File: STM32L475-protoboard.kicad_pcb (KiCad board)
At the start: 4 copper layers, 73.6 x 52.9 mm, 67 parts, among them J1 USB_HEADER, J10 Conn_01x02_Male, J11 SD_Card, J2 USB_B_Micro, J3 DCin, J5 W5500_ETHERNET, J6 STLINK2, J7 BOOT_MODE, J8 Conn_02x20_Odd_Even, J9 Conn_01x02_Male, SW1 RESET, U1 SRV05-4, U2 AMS1117-3.3, U3 STM32L475RCTx, Y1 Crystal_GND24, Y2 32.768k

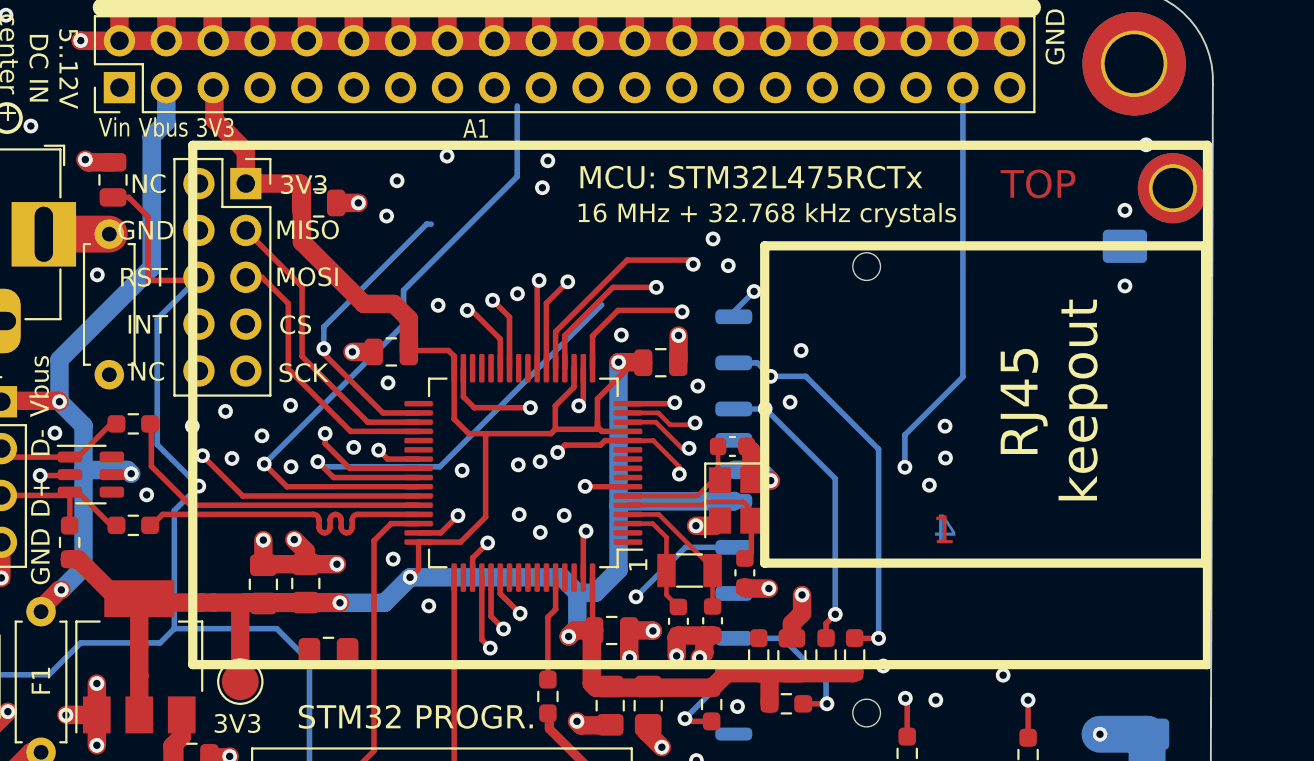
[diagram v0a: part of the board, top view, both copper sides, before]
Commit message: STM32L475 should have internal pullup for USB line, but need to be checked (now DNP resistor)
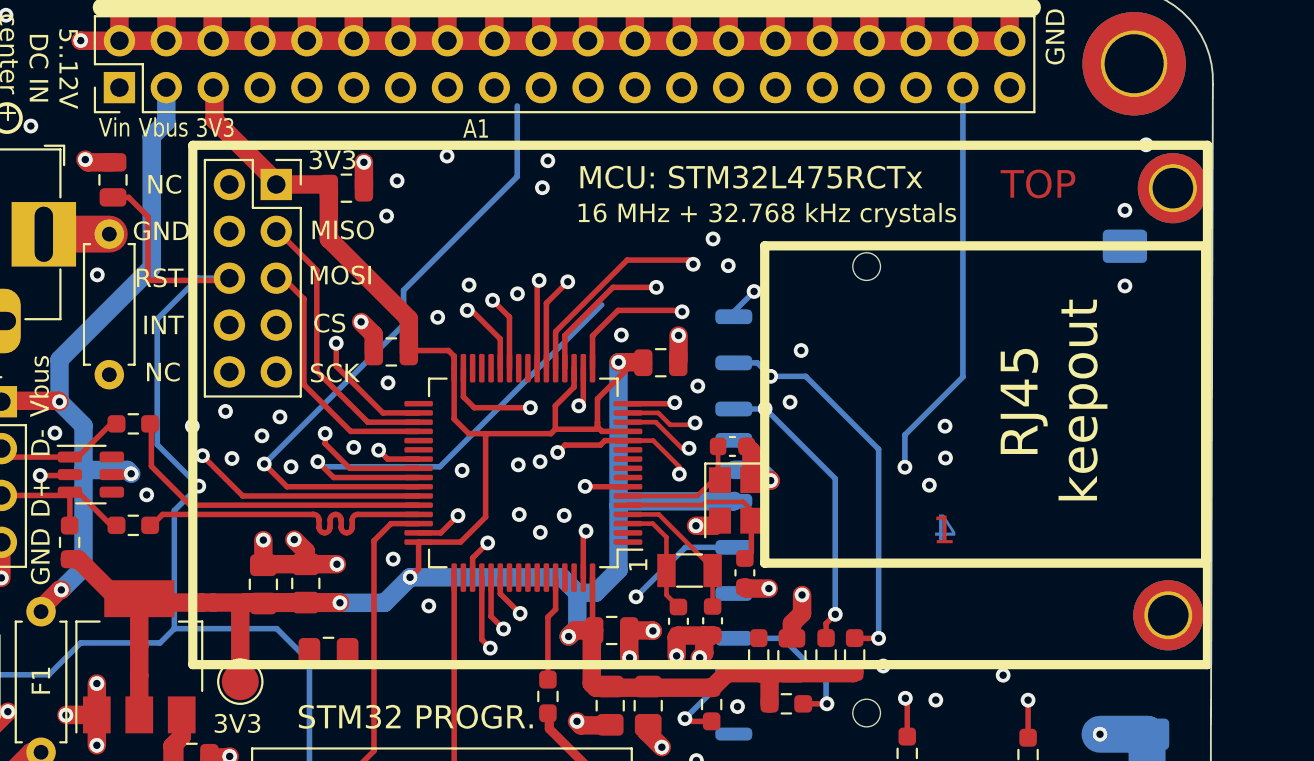
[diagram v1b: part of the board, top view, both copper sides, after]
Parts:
- added H6: MountingHole_Pad, MountingHole:MountingHole_2.2mm_M2_DIN965_Pad_TopBottom, F.Cu at (138.0, 85.8)
- R5: value 1.5k -> DNP
- moved C7 1.70 mm to (93.5, 62.6)
- moved J5 1.65 mm to (89.7, 62.4)
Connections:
- H5 pad 1: unconnected-(H5-Pad1) -> (no net)
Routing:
- net SPI2_SCK: track 20.8 -> 10.7 mm
- net RST: track 98.6 -> 101.9 mm
- net W5500_CS: track 20.3 -> 18.7 mm
- net +3V3: track 182.8 -> 181.7 mm
- net SPI2_MOSI: track 14.9 -> 13.9 mm
- net GND: track 196.4 -> 197.4 mm, vias 139 -> 140
- net SPI2_MISO: track 15.9 -> 15.2 mm
- net W5500_INT: track 19.9 -> 19.3 mm

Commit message: layout
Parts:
- added C9: 10p, Capacitor_SMD:C_0603_1608Metric, F.Cu at (68.6, 95.7)
- added R1: 1k, Resistor_SMD:R_0603_1608Metric_Pad0.98x0.95mm_HandSolder, F.Cu at (71.1, 94.9)
- moved H5 0.20 mm to (138.1, 62.6)
- renumbered C9 to C10, C10 to C11, C11 to C12, C12 to C13, C13 to C14, C14 to C15, C15 to C16, C16 to C17, C17 to C18, C18 to C19, C19 to C20, C20 to C21, C21 to C22, R9 to R10, R10 to R11, R11 to R12, R12 to R13, R1 to R2, R2 to R3, R3 to R4, R4 to R5, R5 to R6, R6 to R7, R7 to R8, R8 to R9
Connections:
- SW1 pad 2: RST -> Net-(C9-Pad1)
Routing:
- net unconnected-(U3-Pad42): track 34.0 -> 8.88 mm
- net unconnected-(U3-Pad41): track 25.0 -> 5.82 mm
- net Net-(C9-Pad1): track 0.00 -> 11.7 mm
- net RST: track 101.9 -> 93.3 mm, vias 2 -> 3
- net GND: track 197.4 -> 199.0 mm, vias 140 -> 141

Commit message: note
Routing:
- net SDMMC1_CLK: track 18.7 -> 21.2 mm
- net SDMMC1_D3: track 53.0 -> 54.5 mm
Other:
- board text added: "RUUVI SD-KORTIN TIELLÄ!"
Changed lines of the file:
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@@
     (effects (font (size 1 1) (thickness 0.25)))
+  )
+  (gr_text "RUUVI SD-KORTIN\nTIELLÄ!" (at 96.35 42.625) (layer "F.SilkS")
+    (effects (font (size 1.5 1.5) (thickness 0.375)))
   )
   (gr_text "Vbus" (at 76.85 73.35 90) (layer "F.SilkS")
@@
   (via (at 94.3 103.2) (size 0.8) (drill 0.4) (layers "F.Cu" "B.Cu") (free) (net 1))
   (via (at 68.3 79.175) (size 0.8) (drill 0.4) (layers "F.Cu" "B.Cu") (net 1))
-  (via (at 118.1 71.425) (size 0.8) (drill 0.4) (layers "F.Cu" "B.Cu") (free) (net 1))
+  (via (at 117.5 70.725) (size 0.8) (drill 0.4) (layers "F.Cu" "B.Cu") (free) (net 1))
   (via (at 85.85 100.4) (size 0.8) (drill 0.4) (layers "F.Cu" "B.Cu") (free) (net 1))
   (via (at 125.05 78.725) (size 0.8) (drill 0.4) (layers "F.Cu" "B.Cu") (free) (net 1))
@@
   (segment (start 96.901 83.7184) (end 105.1306 83.7184) (width 1) (layer "B.Cu") (net 3))
   (segment (start 101.17 96.285) (end 101.17 98.825) (width 1) (layer "B.Cu") (net 3))
-  (segment (start 101.17 91.255) (end 101.17 96.285) (width 1) (layer "B.Cu") (net 3))
   (segment (start 105.9688 86.4562) (end 105.9688 84.5566) (width 1) (layer "B.Cu") (net 3))
   (segment (start 105.9688 84.5566) (end 106.9594 84.5566) (width 1) (layer "B.Cu") (net 3))
+  (segment (start 105.5 86.925) (end 105.5 89.525) (width 1) (layer "B.Cu") (net 3))
   (segment (start 95.5194 85.1) (end 96.901 83.7184) (width 1) (layer "B.Cu") (net 3))
-  (segment (start 105.5 86.925) (end 101.17 91.255) (width 1) (layer "B.Cu") (net 3))
+  (segment (start 101.17 93.855) (end 101.17 96.285) (width 1) (layer "B.Cu") (net 3))
+  (segment (start 105.5 89.525) (end 101.17 93.855) (width 1) (layer "B.Cu") (net 3))
   (segment (start 106.9594 84.5566) (end 108.204 83.312) (width 1) (layer "B.Cu") (net 3))
   (segment (start 105.5 86.925) (end 105.9688 86.4562) (width 1) (layer "B.Cu") (net 3))
@@
   (segment (start 114.45 69.595) (end 114.45 69.325) (width 0.3) (layer "B.Cu") (net 51))
   (segment (start 114.45 69.325) (end 115.55 68.225) (width 0.3) (layer "B.Cu") (net 51))
-  (segment (start 100.7916 87.0966) (end 100.7916 83.7334) (width 0.3) (layer "F.Cu") (net 52))
-  (segment (start 101.25 87.555) (end 101.04 87.555) (width 0.3) (layer "F.Cu") (net 52))
+  (segment (start 100.7916 88.1666) (end 100.7916 83.7334) (width 0.3) (layer "F.Cu") (net 52))
+  (segment (start 100.9 88.275) (end 101.04 88.135) (width 0.3) (layer "F.Cu") (net 52))
   (segment (start 122.3 87.025) (end 121.0125 87.025) (width 0.3) (layer "F.Cu") (net 52))
-  (segment (start 101.25 87.555) (end 100.7916 87.0966) (width 0.3) (layer "F.Cu") (net 52))
   (segment (start 121.0125 87.025) (end 121 87.0125) (width 0.3) (layer "F.Cu") (net 52))
-  (via (at 116.45 72.825) (size 0.8) (drill 0.4) (layers "F.Cu" "B.Cu") (net 52))
-  (via (at 101.25 87.555) (size 0.8) (drill 0.4) (layers "F.Cu" "B.Cu") (net 52))
+  (segment (start 100.9 88.275) (end 100.7916 88.1666) (width 0.3) (layer "F.Cu") (net 52))
+  (via (at 116.2 72.075) (size 0.8) (drill 0.4) (layers "F.Cu" "B.Cu") (net 52))
+  (via (at 100.9 88.275) (size 0.8) (drill 0.4) (layers "F.Cu" "B.Cu") (net 52))
   (via (at 122.3 87.025) (size 0.8) (drill 0.4) (layers "F.Cu" "B.Cu") (net 52))
-  (segment (start 101.25 87.555) (end 101.17048 87.47548) (width 0.3) (layer "In2.Cu") (net 52))
-  (segment (start 101.17048 87.47548) (end 101.17048 84.53452) (width 0.3) (layer "In2.Cu") (net 52))
+  (segment (start 100.9 88.275) (end 100.8 88.175) (width 0.3) (layer "In2.Cu") (net 52))
+  (segment (start 122.3 84.775) (end 122.3 87.025) (width 0.3) (layer "In2.Cu") (net 52))
   (segment (start 102.27 83.435) (end 120.96 83.435) (width 0.3) (layer "In2.Cu") (net 52))
   (segment (start 120.96 83.435) (end 122.3 84.775) (width 0.3) (layer "In2.Cu") (net 52))
-  (segment (start 101.17048 84.53452) (end 102.27 83.435) (width 0.3) (layer "In2.Cu") (net 52))
-  (segment (start 122.3 84.775) (end 122.3 87.025) (width 0.3) (layer "In2.Cu") (net 52))
-  (segment (start 118.35 72.825) (end 122.3 76.775) (width 0.3) (layer "B.Cu") (net 52))
+  (segment (start 100.8 88.175) (end 100.8 84.905) (width 0.3) (layer "In2.Cu") (net 52))
+  (segment (start 100.8 84.905) (end 102.27 83.435) (width 0.3) (layer "In2.Cu") (net 52))
+  (segment (start 116.2 72.075) (end 116.18 72.095) (width 0.3) (layer "B.Cu") (net 52))
   (segment (start 122.3 76.775) (end 122.3 87.025) (width 0.3) (layer "B.Cu") (net 52))
-  (segment (start 114.45 72.095) (end 115.72 72.095) (width 0.3) (layer "B.Cu") (net 52))
-  (segment (start 115.72 72.095) (end 116.45 72.825) (width 0.3) (layer "B.Cu") (net 52))
-  (segment (start 116.45 72.825) (end 118.35 72.825) (width 0.3) (layer "B.Cu") (net 52))
+  (segment (start 116.2 72.075) (end 117.6 72.075) (width 0.3) (layer "B.Cu") (net 52))
+  (segment (start 117.6 72.075) (end 122.3 76.775) (width 0.3) (layer "B.Cu") (net 52))
+  (segment (start 116.18 72.095) (end 114.45 72.095) (width 0.3) (layer "B.Cu") (net 52))
   (segment (start 101.7916 84.608761) (end 101.7916 83.7334) (width 0.3) (layer "F.Cu") (net 53))
   (segment (start 119.95 85.725) (end 119.45 86.225) (width 0.3) (layer "F.Cu") (net 53))
@@
   (segment (start 116.13 74.595) (end 116.15 74.575) (width 0.3) (layer "B.Cu") (net 53))
   (segment (start 119.95 78.375) (end 119.95 85.725) (width 0.3) (layer "B.Cu") (net 53))
-  (segment (start 101.2916 83.7334) (end 101.2916 85.8366) (width 0.3) (layer "F.Cu") (net 54))
-  (segment (start 101.2916 85.8366) (end 101.97 86.515) (width 0.3) (layer "F.Cu") (net 54))
+  (segment (start 102.55 87.525) (end 101.2916 86.2666) (width 0.3) (layer "F.Cu") (net 54))
+  (segment (start 101.2916 86.2666) (end 101.2916 83.7334) (width 0.3) (layer "F.Cu") (net 54))
   (via (at 109.15 84.775) (size 0.8) (drill 0.4) (layers "F.Cu" "B.Cu") (net 54))
-  (via (at 101.97 86.515) (size 0.8) (drill 0.4) (layers "F.Cu" "B.Cu") (net 54))
-  (segment (start 101.67 86.215) (end 101.97 86.515) (width 0.3) (layer "In2.Cu") (net 54))
-  (segment (start 101.67 85.335) (end 101.67 86.215) (width 0.3) (layer "In2.Cu") (net 54))
-  (segment (start 102.44 84.565) (end 101.67 85.335) (width 0.3) (layer "In2.Cu") (net 54))
-  (segment (start 108.94 84.565) (end 102.44 84.565) (width 0.3) (layer "In2.Cu") (net 54))
-  (segment (start 109.15 84.775) (end 108.94 84.565) (width 0.3) (layer "In2.Cu") (net 54))
+  (via (at 102.55 87.525) (size 0.8) (drill 0.4) (layers "F.Cu" "B.Cu") (net 54))
+  (segment (start 101.67 85.335) (end 102.44 84.565) (width 0.3) (layer "In2.Cu") (net 54))
+  (segment (start 101.67 86.645) (end 101.67 85.335) (width 0.3) (layer "In2.Cu") (net 54))
+  (segment (start 108.94 84.565) (end 109.15 84.775) (width 0.3) (layer "In2.Cu") (net 54))
+  (segment (start 102.44 84.565) (end 108.94 84.565) (width 0.3) (layer "In2.Cu") (net 54))
+  (segment (start 102.55 87.525) (end 101.67 86.645) (width 0.3) (layer "In2.Cu") (net 54))
   (segment (start 109.15 84.775) (end 111.83 82.095) (width 0.3) (layer "B.Cu") (net 54))
   (segment (start 111.83 82.095) (end 114.45 82.095) (width 0.3) (layer "B.Cu") (net 54))

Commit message: some fixes
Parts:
- moved R2 3.69 mm to (117.2, 96.2), turned to -90 degrees
- moved D3 3.21 mm to (117.2, 99.6), turned to 90 degrees
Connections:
- J7 pad 1: +3V3 -> GND
- J7 pad 3: GND -> +3V3
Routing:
- net +3V3: track 181.8 -> 180.5 mm
- net GND: vias 141 -> 142

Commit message: some routing
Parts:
- C1, C4, C5: value 100u -> 22u
- C11, C19: value 10u -> 22u
- C16: value 10u -> 100n
- Y1: value Crystal_GND24 -> 16 MHz
- moved C19 6.63 mm to (87.0, 84.1), turned to -90 degrees
- moved R9 1.91 mm to (115.8, 89.8), turned to 90 degrees
- moved R2 1.37 mm to (116.2, 97.1), turned to 0 degrees
- moved R10 0.96 mm to (117.8, 91.4), turned to -90 degrees
- moved C21 0.69 mm to (110.5, 90.7)
- moved R6 0.41 mm to (78.8, 81.9)
- moved C20 0.30 mm to (107.5, 90.7)
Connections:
- C19 pad 1: unconnected-(C19-Pad1) -> GND
- C19 pad 2: unconnected-(C19-Pad2) -> +3V3
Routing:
- net SDMMC1_D1: track 11.4 -> 51.6 mm
- net SDMMC1_D0: track 10.9 -> 49.8 mm, vias 2 -> 3
- net SDMMC1_D2: track 28.8 -> 58.3 mm, vias 2 -> 3
- net +VDC: track 36.6 -> 54.4 mm
- net GND: track 199.0 -> 196.5 mm, vias 142 -> 146
- net +3V3: track 180.5 -> 182.8 mm, vias 4 -> 5
- net /USB_ID: track 12.6 -> 14.7 mm, vias 1 -> 2
- net RST: track 93.3 -> 94.9 mm
- net SDMMC1_CMD: track 35.7 -> 36.8 mm

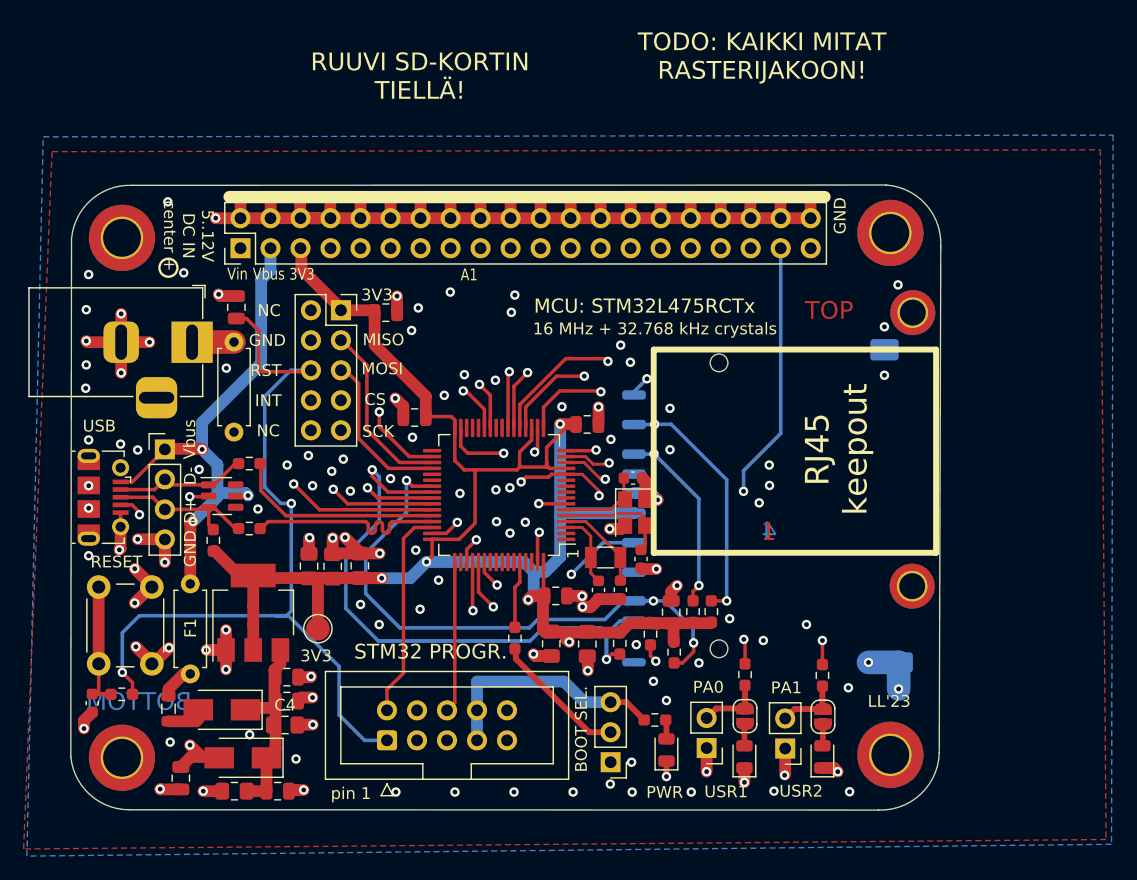
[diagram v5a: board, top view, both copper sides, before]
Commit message: some more pins
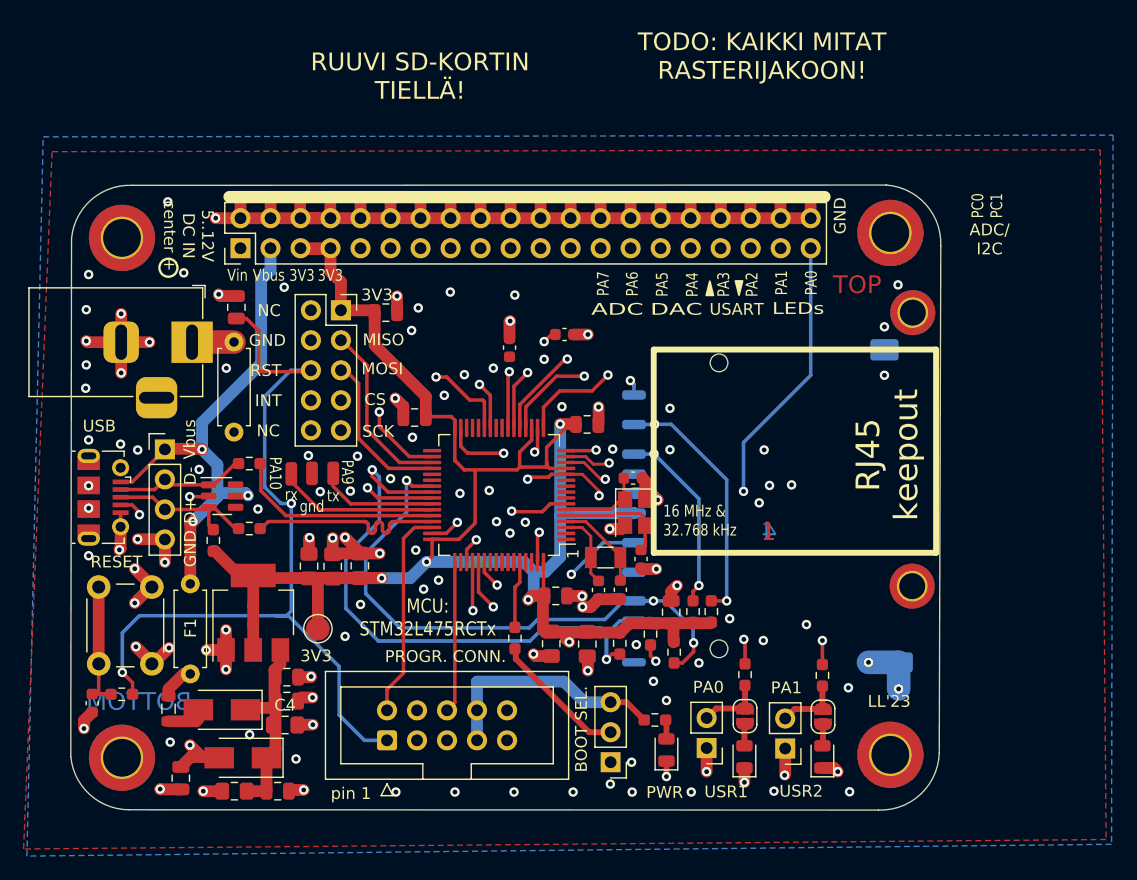
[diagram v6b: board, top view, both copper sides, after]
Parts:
- added C20: 12p, Capacitor_SMD:C_0603_1608Metric, F.Cu at (108.6, 64.5)
- added C21: 12p, Capacitor_SMD:C_0603_1608Metric, F.Cu at (103.9, 65.6)
- added J10: GNDPAD, Connector_Wire:SolderWirePad_1x01_SMD_1x2mm, F.Cu at (87.2, 76.2)
- added J8: PAD_PA9_USART1_TX, Connector_Wire:SolderWirePad_1x01_SMD_1x2mm, F.Cu at (89.0, 76.2)
- added J9: PAD_PA10_USART1_RX, Connector_Wire:SolderWirePad_1x01_SMD_1x2mm, F.Cu at (85.5, 76.3)
- renumbered C11 to C10, C12 to C11, C13 to C12, C7 to C13, C19 to C18, C18 to C19, C20 to C22, C21 to C23, C22 to C24, C8 to C7, C9 to C8, C10 to C9, J9 to J11, J10 to J12, J8 to J13, J11 to J14, R3 to R2, R4 to R3, R5 to R4, R6 to R5, R2 to R6
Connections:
- net /USB_ID renamed PA10
- J13 pad 25: unconnected-(J8-Pad25) -> PA7
- J13 pad 27: unconnected-(J8-Pad27) -> PA6
- J13 pad 29: unconnected-(J8-Pad29) -> PA5
- J13 pad 31: unconnected-(J8-Pad31) -> PA4
- J13 pad 33: unconnected-(J8-Pad33) -> PA3
- J13 pad 35: unconnected-(J8-Pad35) -> PA2
- J13 pad 37: LED_USR1 -> LED_USR2
- J13 pad 39: LED_USR2 -> LED_USR1
- J13 pad 7: unconnected-(J8-Pad7) -> +3V3
- U3 pad 16: unconnected-(U3-Pad16) -> PA2
- U3 pad 17: unconnected-(U3-Pad17) -> PA3
- U3 pad 20: unconnected-(U3-Pad20) -> PA4
- U3 pad 21: unconnected-(U3-Pad21) -> PA5
- U3 pad 22: unconnected-(U3-Pad22) -> PA6
- U3 pad 23: unconnected-(U3-Pad23) -> PA7
- U3 pad 42: unconnected-(U3-Pad42) -> PA9
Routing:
- net PA2: track 0.00 -> 25.3 mm, vias 0 -> 1
- net PA3: track 0.00 -> 23.1 mm, vias 0 -> 1
- net PA4: track 0.00 -> 22.4 mm, vias 0 -> 1
- net PA5: track 0.00 -> 21.1 mm, vias 0 -> 1
- net PA6: track 0.00 -> 20.6 mm, vias 0 -> 2
- net PA7: track 0.00 -> 18.5 mm, vias 0 -> 1
- net unconnected-(U3-Pad21): track 17.2 -> 0.00 mm, vias 1 -> 0
- net unconnected-(U3-Pad22): track 15.4 -> 0.00 mm, vias 1 -> 0
- net unconnected-(U3-Pad23): track 14.0 -> 0.00 mm, vias 1 -> 0
- net unconnected-(U3-Pad20): track 10.5 -> 0.00 mm, vias 1 -> 0
- net PA9: track 0.00 -> 10.1 mm
- net unconnected-(U3-Pad42): track 8.88 -> 0.00 mm, vias 1 -> 0
- net unconnected-(U3-Pad17): track 8.16 -> 0.00 mm, vias 1 -> 0
- net +3V3: track 182.8 -> 186.9 mm
- net unconnected-(U3-Pad16): track 2.76 -> 0.00 mm, vias 1 -> 0
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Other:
- board text added: "16 MHz & 32.768 kHz"
- board text added: "ADC"
- board text added: "ADC/ I2C"
- board text added: "DAC"
- board text added: "LEDs"
- board text added: "PA10"
- board text added: "PA2"
- board text added: "PA3"
- board text added: "PA4"
- board text added: "PA5"
- board text added: "PA6"
- board text added: "PA7"
- board text added: "PA9"
- board text added: "PC0"
- board text added: "PC1"
- board text added: "PROGR. CONN."
- board text added: "USART"
- board text added: "gnd"
- board text added: "rx"
- board text added: "tx"
- board text removed: "16 MHz + 32.768 kHz crystals"
- board text removed: "A1"
- board text removed: "STM32 PROGR."

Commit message: texts
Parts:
- C20, C21: value 12p -> DNP; footprint Capacitor_SMD:C_0603_1608Metric -> Capacitor_SMD:C_0805_2012Metric_Pad1.18x1.45mm_HandSolder
- moved C21 0.51 mm to (103.9, 65.1)
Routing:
- net GND: track 198.6 -> 200.6 mm
